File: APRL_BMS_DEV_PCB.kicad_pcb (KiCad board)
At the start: 4 copper layers, 73 parts, among them J1 Conn_01x04_Pin, J3 Conn_01x02_Pin, J4 Conn_01x08_Pin, J5 Conn_01x01_Pin, Q1 Q_NPN, SW1 SW_SPDT, U1 BQ756506-Q1, U2 STM32F446RCTx, U3 ISO7741DWR, Y1 20MHz

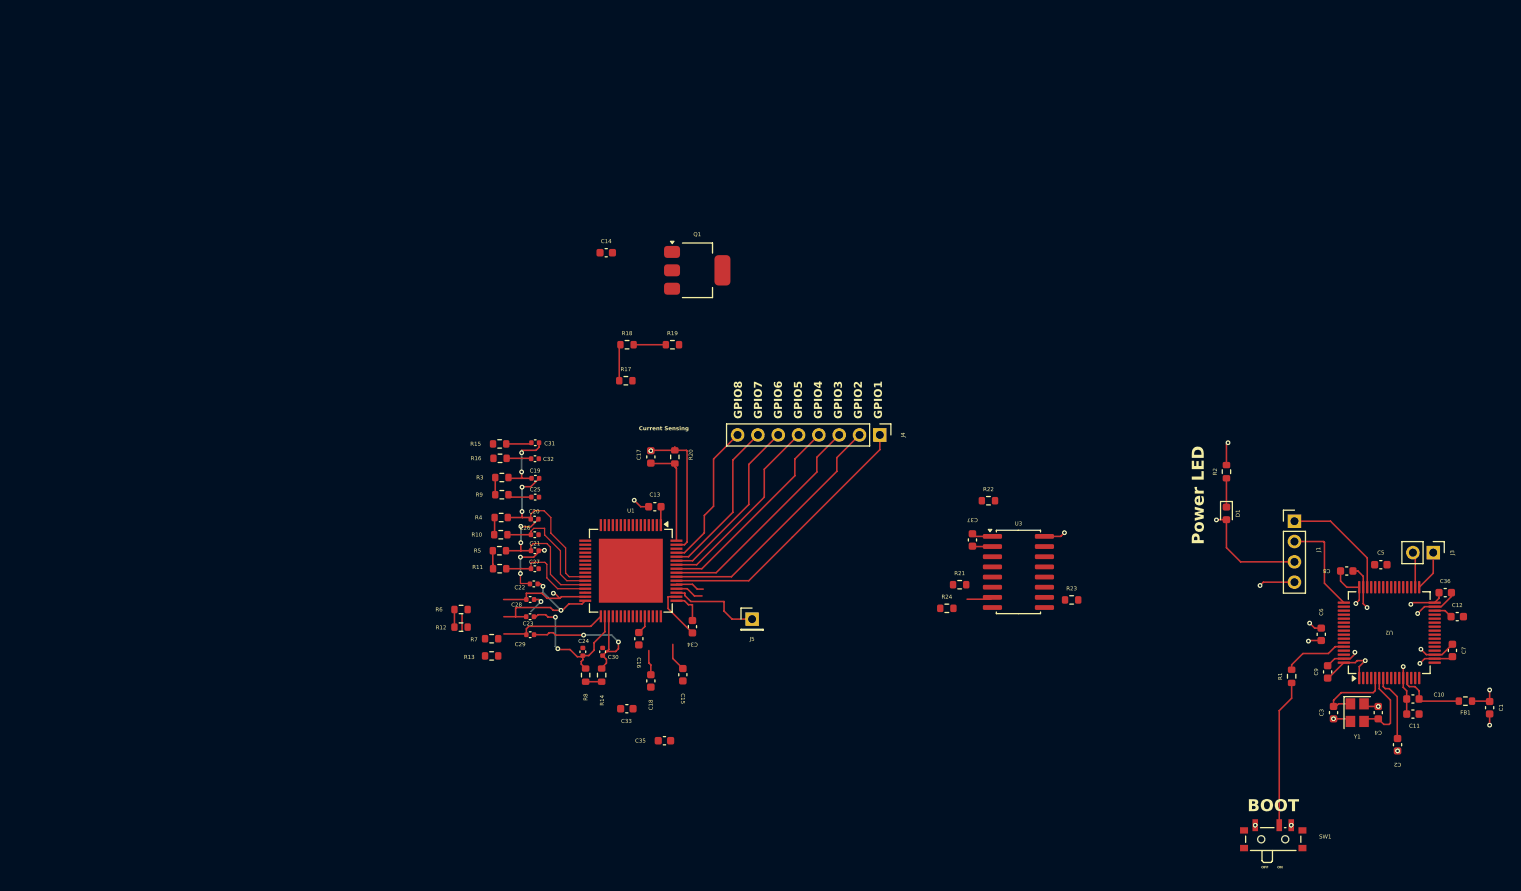
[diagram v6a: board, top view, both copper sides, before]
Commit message: Finished sketching traces - save for NPN
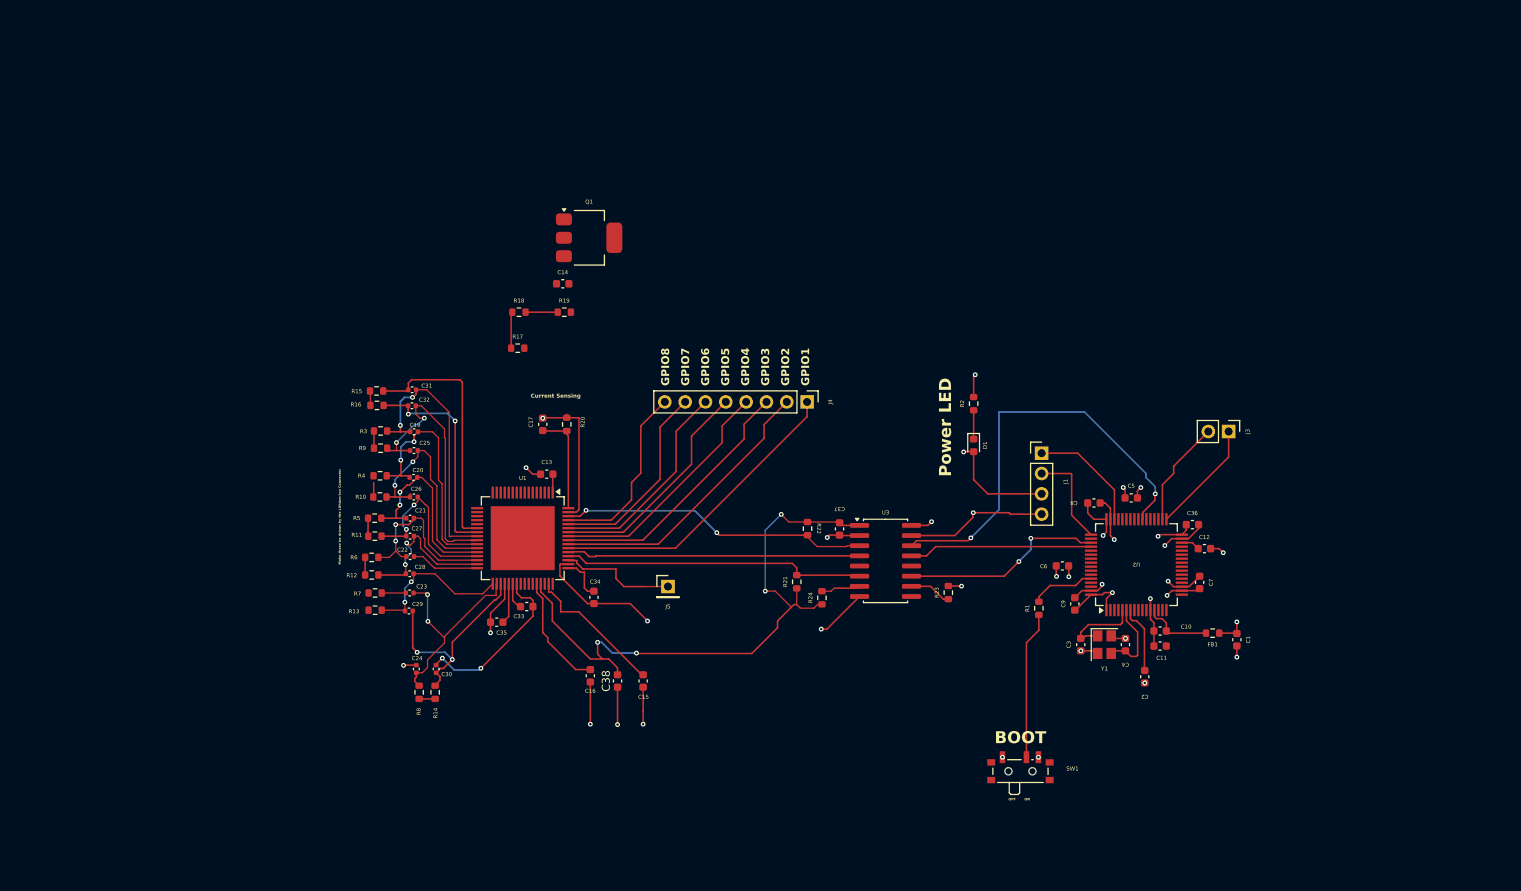
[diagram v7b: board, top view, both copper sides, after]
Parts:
- removed C18: 10u, Capacitor_SMD:C_0603_1608Metric
- added C38: 10u, Capacitor_SMD:C_0603_1608Metric, F.Cu at (123.1, 114.0)
- moved C6 33.5 mm to (178.8, 99.7), turned to 180 degrees
- moved C2 32.7 mm to (189.0, 113.5)
- moved C7 32.7 mm to (195.9, 101.7)
- moved SW1 32.7 mm to (173.5, 125.0)
- moved C1 32.7 mm to (200.6, 108.9)
- moved C10 32.7 mm to (191.0, 107.8)
- moved C11 32.7 mm to (191.0, 109.7)
- moved C12 32.7 mm to (196.5, 97.5)
- moved C3 32.7 mm to (181.0, 109.5)
- moved C36 32.7 mm to (195.0, 94.5)
- moved C4 32.7 mm to (186.6, 109.5)
- moved C8 32.7 mm to (182.7, 91.8)
- moved C9 32.7 mm to (180.3, 104.4)
- moved D1 32.7 mm to (167.7, 84.6)
- moved FB1 32.7 mm to (197.5, 108.0)
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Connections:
- C16 pad 1: /CVSS -> GND
- C33 pad 1: /AVSS -> GND
- C34 pad 2: /DVSS -> GND
- C35 pad 1: /REFHP -> GND
- C35 pad 2: /REFHM -> /REFHP
- U1 pad 36: /REFHM -> GND
- U1 pad 39: /AVSS -> GND
- U1 pad 46: /CVSS -> GND
- U1 pad 50: /DVSS -> GND
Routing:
- net GND: track 64.2 -> 149.2 mm, vias 15 -> 27
- net /CVDD: track 5.77 -> 78.0 mm, vias 0 -> 4
- net /NFAULT_IN: track 0.00 -> 53.5 mm, vias 0 -> 2
- net /NFAULT: track 0.00 -> 38.8 mm, vias 0 -> 2
- net /RX_BMS: track 3.57 -> 38.0 mm
- net /TX_BMS: track 3.62 -> 36.7 mm
- net /VC5: track 2.99 -> 34.7 mm, vias 0 -> 2
- net /CB6: track 3.21 -> 31.1 mm
- net /UART_TX: track 0.00 -> 25.4 mm, vias 0 -> 2
- net /CB5: track 9.33 -> 34.0 mm
- net /VC6: track 3.09 -> 27.1 mm, vias 0 -> 2
- net /UART_RX: track 0.00 -> 22.9 mm
- net /LDOIN: track 3.54 -> 17.9 mm
- net /CB2: track 8.03 -> 22.2 mm, vias 3 -> 2
- net /VC4: track 15.2 -> 28.4 mm, vias 0 -> 2
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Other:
- board text added: "Make these be driven by the Lithium-Ion Connector"

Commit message: Finished initial trace.
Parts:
- removed Q1: Q_NPN, Package_TO_SOT_SMD:SOT-223
- added Q2: NPN, Package_TO_SOT_SMD:SOT-23, F.Cu at (121.5, 72.0)
- U1: footprint Package_QFP:HTQFP-64-1EP_10x10mm_P0.5mm_EP8x8mm -> Package_QFP:LQFP-64_10x10mm_P0.5mm
- moved C14 8.46 mm to (108.4, 61.4)
- moved C1 6.25 mm to (199.6, 102.7)
- moved C15 6.25 mm to (125.4, 107.8)
- moved C29 6.25 mm to (96.1, 99.1)
- moved C30 6.25 mm to (99.5, 106.3)
- moved C38 6.25 mm to (122.2, 107.8)
- moved C6 6.25 mm to (177.8, 93.5)
- moved C9 6.25 mm to (179.4, 98.2)
- moved J1 6.25 mm to (175.2, 79.4)
- moved J4 6.25 mm to (145.9, 73.0)
- moved J5 6.25 mm to (128.5, 96.0)
- moved R1 6.25 mm to (174.9, 98.8)
- moved R10 6.25 mm to (92.5, 84.8)
- moved R11 6.25 mm to (91.9, 89.8)
- moved R13 6.25 mm to (91.9, 99.0)
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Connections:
- net Net-(C14-Pad2) renamed /Collector
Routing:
- net /CELL_0: track 14.8 -> 65.5 mm, vias 0 -> 2
- net /NPNB: track 0.00 -> 34.8 mm, vias 0 -> 2
- net /LDOIN: track 17.9 -> 46.6 mm, vias 0 -> 2
- net /CELL_6: track 6.38 -> 24.6 mm
- net /Collector: track 0.00 -> 17.7 mm
- net /BAT: track 2.31 -> 17.7 mm
- net GND: track 149.2 -> 151.0 mm, vias 27 -> 28
- net /CVDD: track 78.0 -> 79.4 mm
- net /NFAULT: track 38.8 -> 40.0 mm
- net /NEG5V: track 14.6 -> 15.8 mm
